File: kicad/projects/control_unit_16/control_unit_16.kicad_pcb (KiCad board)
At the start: 2 copper layers, 203.2 x 97.8 mm, 54 parts, among them J1 Conn_01x04_Female, J2 Control_signal_backplane, J3 Bus_connection, J4 Aux_connection, J5 Conn_01x16_Female, U1 74HCT04, U10 28C256, U11 28C256, U2 28C256, U3 74HCT173, U4 74HCT377, U5 74HCT161, U6 28C256, U7 74HCT245, U8 74HCT245, U9 74HCT138

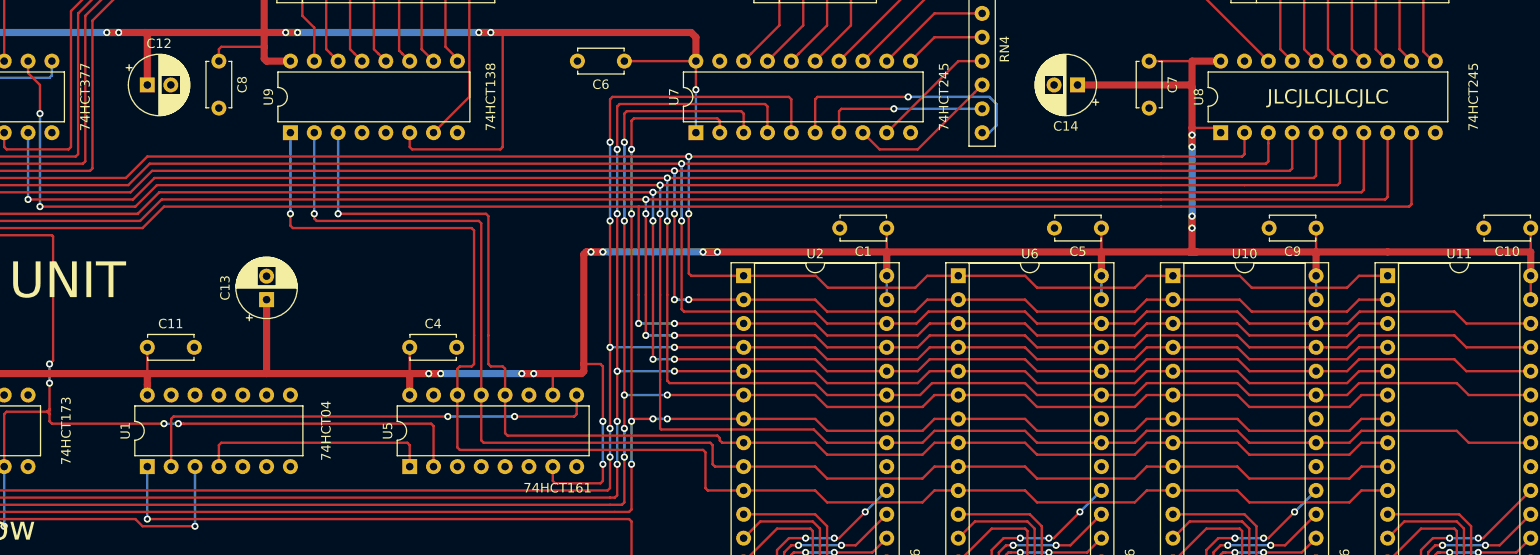
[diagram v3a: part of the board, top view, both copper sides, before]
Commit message: Switch to HC series chips and fix some labelling in program counter or register PCB.
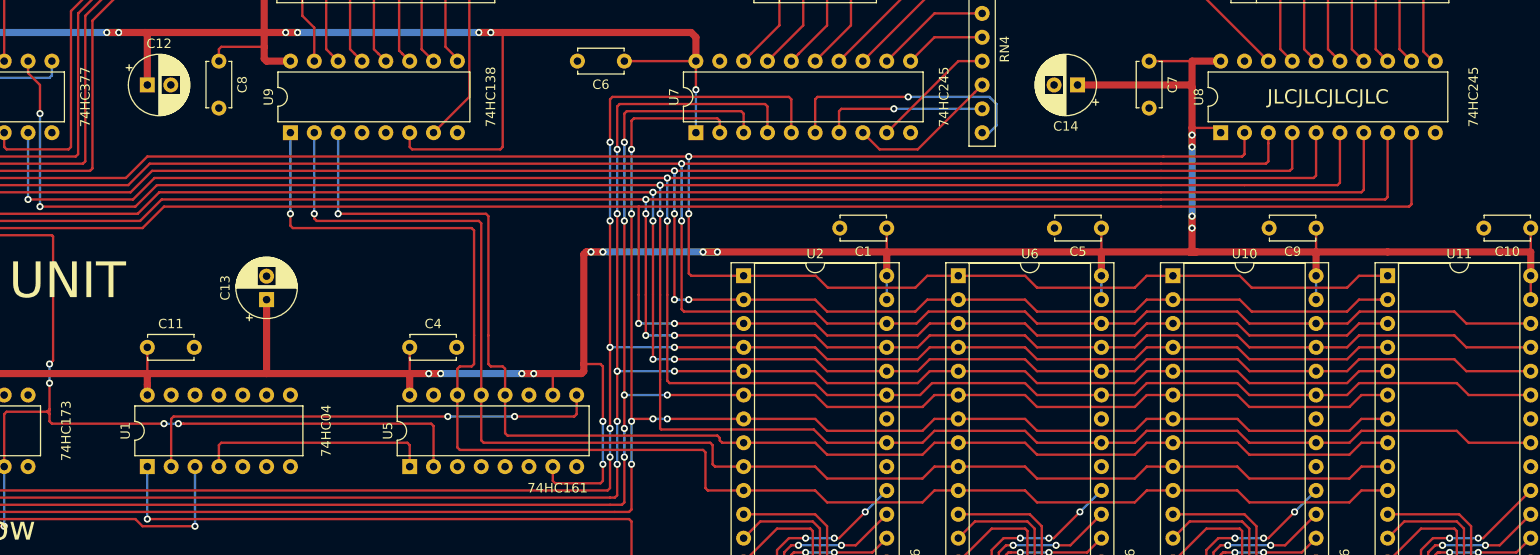
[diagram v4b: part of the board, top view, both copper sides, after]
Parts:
- U1: value 74HCT04 -> 74HC04
- U3: value 74HCT173 -> 74HC173
- U4: value 74HCT377 -> 74HC377
- U5: value 74HCT161 -> 74HC161
- U7, U8: value 74HCT245 -> 74HC245
- U9: value 74HCT138 -> 74HC138
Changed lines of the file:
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@@
       (effects (font (size 1 1) (thickness 0.15)))
     )
-    (fp_text value 74HCT138 (at 3.81 21.336 90) (layer F.SilkS)
+    (fp_text value 74HC138 (at 3.81 21.336 90) (layer F.SilkS)
       (effects (font (size 1.016 1.016) (thickness 0.1778)))
     )
@@
       (effects (font (size 1 1) (thickness 0.15)))
     )
-    (fp_text value 74HCT245 (at 3.81 26.924 90) (layer F.SilkS)
+    (fp_text value 74HC245 (at 3.81 26.924 90) (layer F.SilkS)
       (effects (font (size 1.016 1.016) (thickness 0.1778)))
     )
@@
       (effects (font (size 1 1) (thickness 0.15)))
     )
-    (fp_text value 74HCT245 (at 3.81 26.416 90) (layer F.SilkS)
+    (fp_text value 74HC245 (at 3.81 26.416 90) (layer F.SilkS)
       (effects (font (size 1.016 1.016) (thickness 0.1778)))
     )
@@
       (effects (font (size 1 1) (thickness 0.15)))
     )
-    (fp_text value 74HCT161 (at -2.286 15.748 180) (layer F.SilkS)
+    (fp_text value 74HC161 (at -2.286 15.748 180) (layer F.SilkS)
       (effects (font (size 1.016 1.016) (thickness 0.1778)))
     )
@@
       (effects (font (size 1 1) (thickness 0.15)))
     )
-    (fp_text value 74HCT377 (at 3.81 26.416 90) (layer F.SilkS)
+    (fp_text value 74HC377 (at 3.81 26.416 90) (layer F.SilkS)
       (effects (font (size 1.016 1.016) (thickness 0.1778)))
     )
@@
       (effects (font (size 1 1) (thickness 0.15)))
     )
-    (fp_text value 74HCT173 (at 3.81 21.844 90) (layer F.SilkS)
+    (fp_text value 74HC173 (at 3.81 21.844 90) (layer F.SilkS)
       (effects (font (size 1.016 1.016) (thickness 0.1778)))
     )
@@
       (effects (font (size 1 1) (thickness 0.15)))
     )
-    (fp_text value 74HCT04 (at 3.81 19.05 90) (layer F.SilkS)
-      (effects (font (size 1.016 1.016) (thickness 0.1778)))
-    )
+    (fp_text value 74HC04 (at 3.81 19.05 90) (layer F.SilkS)
+      (effects (font (size 1.016 1.016) (thickness 0.1778)))
+    )

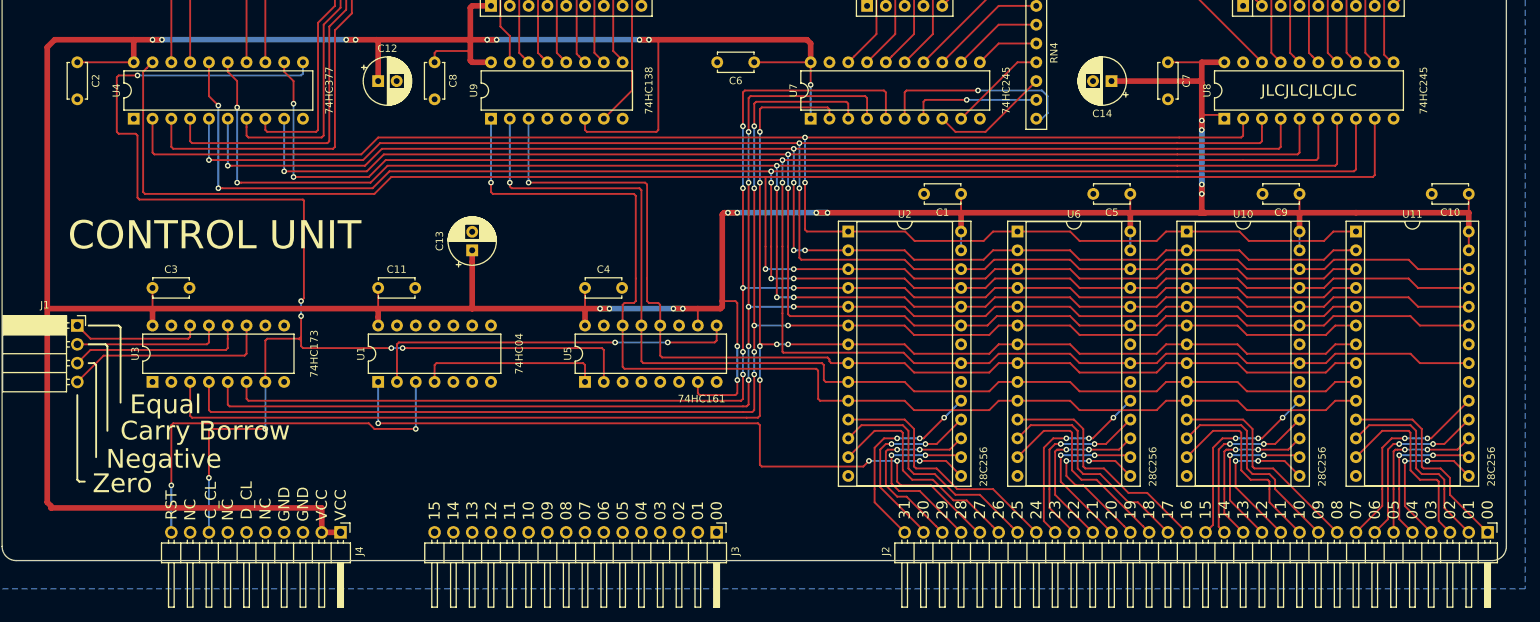
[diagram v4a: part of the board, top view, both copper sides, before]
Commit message: Adjust lower connector position on control unit.
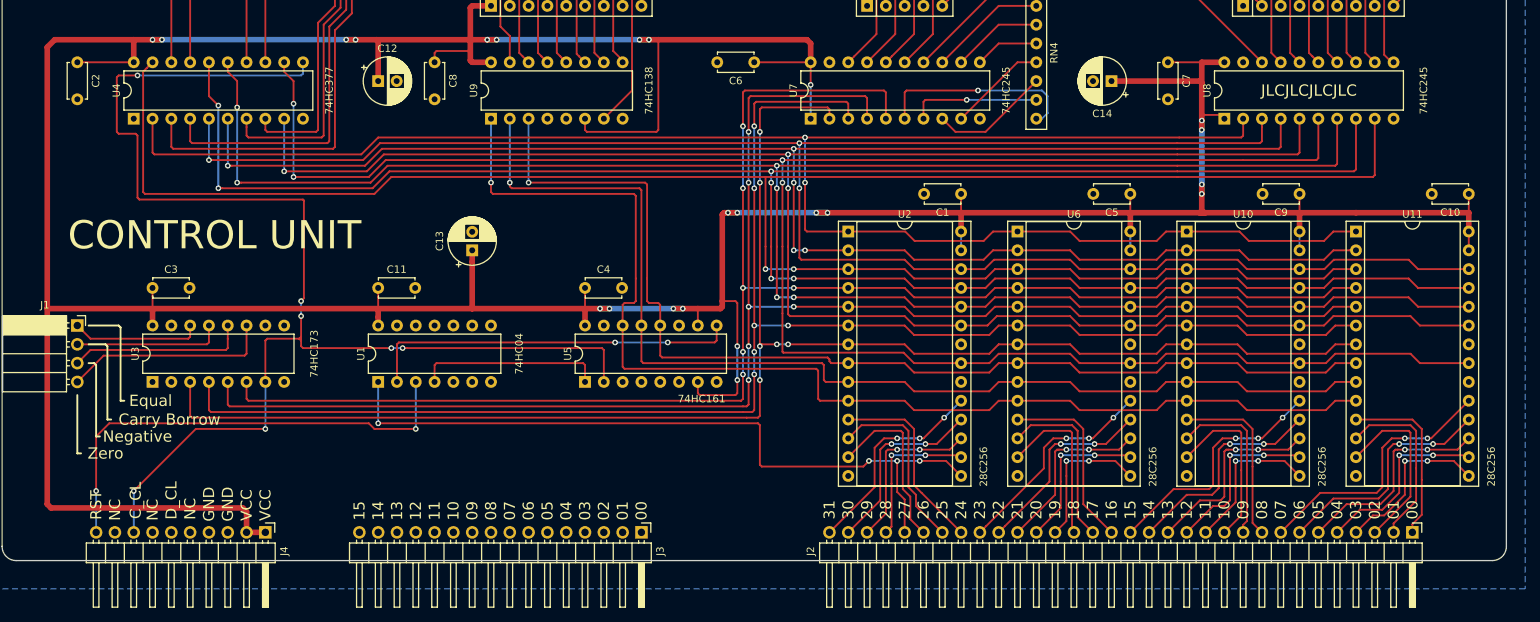
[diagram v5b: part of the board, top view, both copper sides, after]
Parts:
- moved J2 10.2 mm to (241.3, 144.8)
- moved J3 10.2 mm to (137.2, 144.8)
- moved J4 10.2 mm to (86.4, 144.8)
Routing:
- net VCC: track 626.3 -> 615.8 mm
- net /RESET: track 54.3 -> 63.5 mm
- net /ROM_3_0: track 34.7 -> 26.0 mm
- net /ROM_0_7: track 27.2 -> 35.9 mm
- net /ROM_0_6: track 24.5 -> 32.3 mm
- net /ROM_3_1: track 32.6 -> 24.8 mm
- net /ROM_2_0: track 32.1 -> 25.0 mm
- net /ROM_1_7: track 26.2 -> 33.2 mm
- net /ROM_3_2: track 30.5 -> 23.6 mm
- net /ROM_0_5: track 21.8 -> 28.7 mm
- net /STEP_RESET: track 107.8 -> 101.1 mm
- net /ROM_2_1: track 30.0 -> 23.7 mm
- net /ROM_1_0: track 29.6 -> 23.9 mm
- net /ROM_1_6: track 24.1 -> 29.7 mm
- net /CONTROL_CLOCK: track 172.3 -> 177.7 mm
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
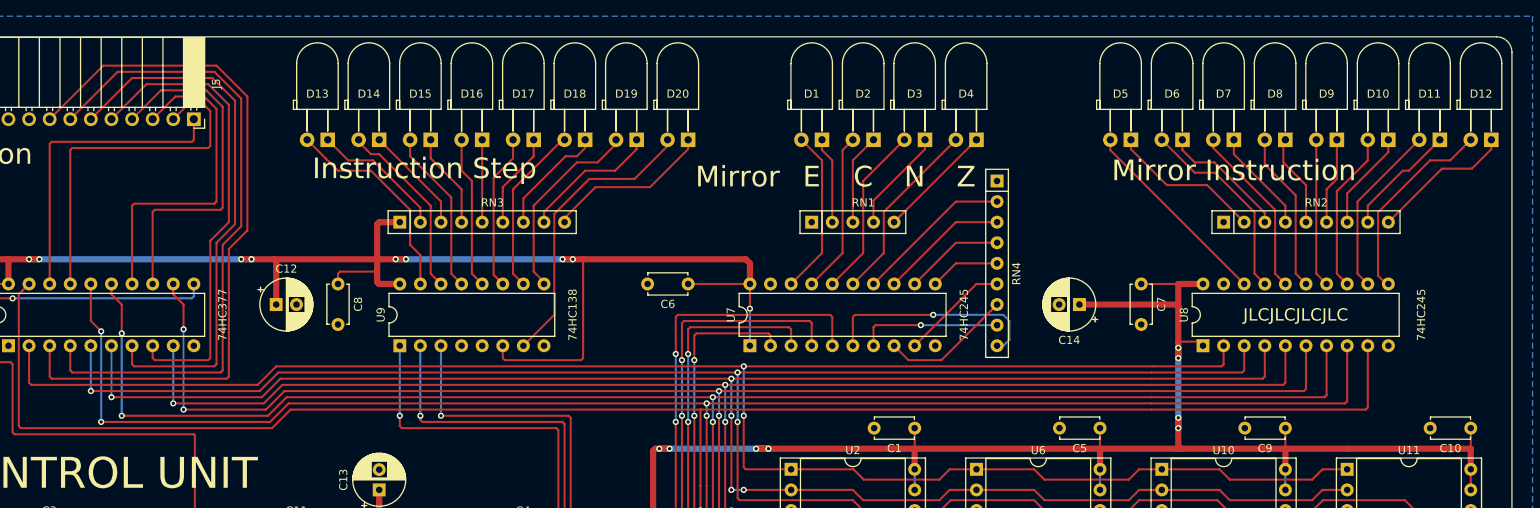
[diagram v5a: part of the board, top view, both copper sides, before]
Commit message: Add top power and LED control to control unit.
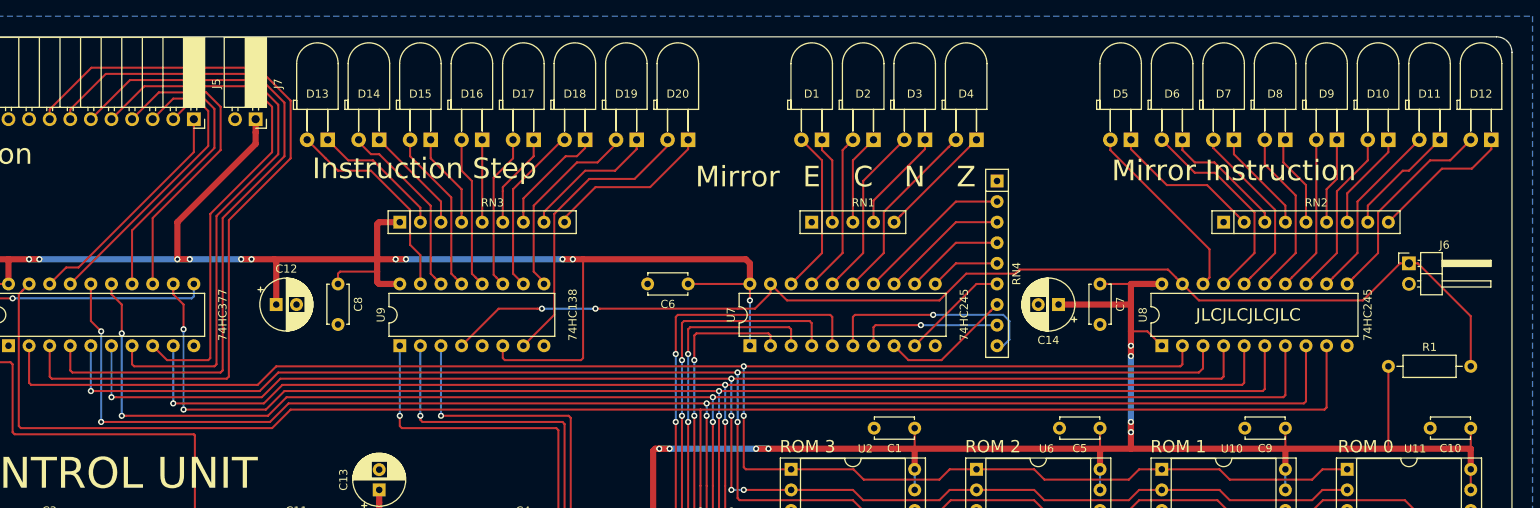
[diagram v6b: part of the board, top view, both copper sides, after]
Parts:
- added J6: LED_CONTROL, Connector_PinHeader_2.54mm:PinHeader_1x02_P2.54mm_Horizontal, F.Cu at (241.3, 78.7)
- added J7: TOP_POWER, Connector_PinSocket_2.54mm:PinSocket_1x02_P2.54mm_Horizontal, F.Cu at (99.1, 61.0)
- added R1: R_US, Resistor_THT:R_Axial_DIN0207_L6.3mm_D2.5mm_P10.16mm_Horizontal, F.Cu at (238.8, 91.4)
- moved C7 5.08 mm to (203.2, 81.3)
- moved U8 5.08 mm to (210.8, 88.9)
- moved C14 2.58 mm to (198.1, 83.8)
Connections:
- U7 pad 19: GND -> /LED_CONTROL
- U8 pad 19: GND -> /LED_CONTROL
- U9 pad 4: GND -> /LED_CONTROL
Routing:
- net /LED_CONTROL: track 0.00 -> 143.1 mm, vias 0 -> 2
- net VCC: track 615.8 -> 645.8 mm, vias 23 -> 25
- net /INST_01: track 44.1 -> 33.8 mm
- net /INST_00: track 37.8 -> 28.6 mm
- net /INST_06: track 81.4 -> 89.1 mm
- net /INST_07: track 90.3 -> 98.0 mm
- net /INST_05: track 67.4 -> 74.4 mm
- net /INST_02: track 41.4 -> 35.0 mm
- net /INST_04: track 58.4 -> 64.6 mm
- net /INST_03: track 43.7 -> 38.3 mm
- net /MIR_INST_6: track 261.6 -> 256.4 mm
- net /MIR_INST_5: track 246.3 -> 241.2 mm
- net /MIR_INST_4: track 267.2 -> 262.1 mm
- net /MIR_INST_2: track 287.5 -> 282.4 mm
- net /MIR_INST_1: track 291.8 -> 286.7 mm
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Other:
- board text added: "ROM 0"
- board text added: "ROM 1"
- board text added: "ROM 2"
- board text added: "ROM 3"

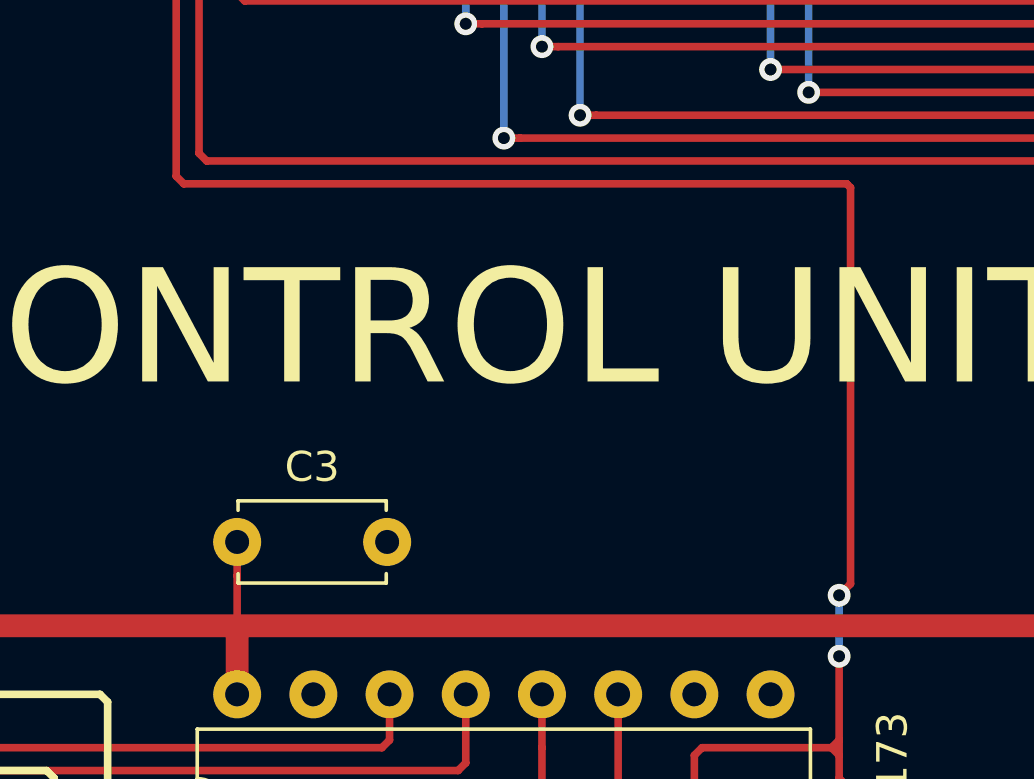
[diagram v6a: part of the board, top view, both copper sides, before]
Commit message: Add top power and LED control to program counter.
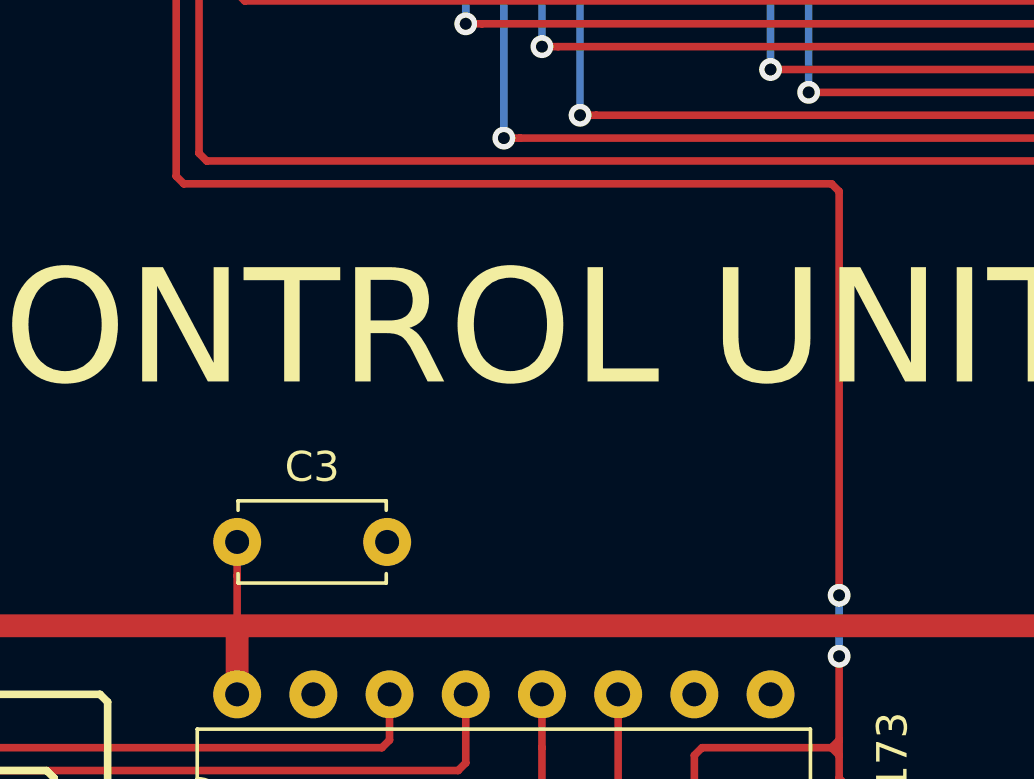
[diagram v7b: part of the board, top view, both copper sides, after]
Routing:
- net /CONTROL_CLOCK: track 177.7 -> 177.1 mm
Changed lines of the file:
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@@
     (thickness 1.6)
     (drawings 40)
-    (tracks 1318)
+    (tracks 1317)
     (zones 0)
     (modules 57)
@@
   (via (at 91.186 113.538) (size 0.762) (drill 0.4) (layers F.Cu B.Cu) (net 98))
   (segment (start 91.186 115.57) (end 91.186 113.538) (width 0.254) (layer B.Cu) (net 98))
-  (segment (start 91.566999 113.157001) (end 91.566999 99.948999) (width 0.254) (layer F.Cu) (net 98))
-  (segment (start 91.186 113.538) (end 91.566999 113.157001) (width 0.254) (layer F.Cu) (net 98))
-  (segment (start 91.566999 99.948999) (end 91.44 99.822) (width 0.254) (layer F.Cu) (net 98))
-  (segment (start 91.44 99.822) (end 69.342 99.822) (width 0.254) (layer F.Cu) (net 98))
-  (segment (start 69.342 99.822) (end 69.088 99.568) (width 0.254) (layer F.Cu) (net 98))
-  (segment (start 69.088 99.568) (end 69.088 91.186) (width 0.254) (layer F.Cu) (net 98))
-  (segment (start 69.088 91.186) (end 68.834 90.932) (width 0.254) (layer F.Cu) (net 98))
-  (segment (start 68.834 90.932) (end 66.548 90.932) (width 0.254) (layer F.Cu) (net 98))
-  (segment (start 66.548 90.932) (end 66.294 90.678) (width 0.254) (layer F.Cu) (net 98))
-  (segment (start 66.294 90.678) (end 66.294 83.312) (width 0.254) (layer F.Cu) (net 98))
-  (segment (start 66.294 83.312) (end 66.548 83.058) (width 0.254) (layer F.Cu) (net 98))
   (via (at 69.088 83.058) (size 0.762) (drill 0.4) (layers F.Cu B.Cu) (net 98))
-  (segment (start 66.548 83.058) (end 69.088 83.058) (width 0.254) (layer F.Cu) (net 98))
   (segment (start 69.088 83.058) (end 91.186 83.058) (width 0.254) (layer B.Cu) (net 98))
   (segment (start 91.186 83.058) (end 91.44 82.804) (width 0.254) (layer B.Cu) (net 98))
@@
   (segment (start 76.962 130.81) (end 68.579992 139.192008) (width 0.254) (layer F.Cu) (net 98))
   (segment (start 68.58 139.192008) (end 68.58 144.78) (width 0.254) (layer B.Cu) (net 98))
+  (segment (start 66.548 90.932) (end 66.294 90.678) (width 0.254) (layer F.Cu) (net 98))
+  (segment (start 91.186 100.076) (end 90.932 99.822) (width 0.254) (layer F.Cu) (net 98))
+  (segment (start 66.294 83.312) (end 66.548 83.058) (width 0.254) (layer F.Cu) (net 98))
+  (segment (start 69.342 99.822) (end 69.088 99.568) (width 0.254) (layer F.Cu) (net 98))
+  (segment (start 69.088 99.568) (end 69.088 91.186) (width 0.254) (layer F.Cu) (net 98))
+  (segment (start 66.548 83.058) (end 69.088 83.058) (width 0.254) (layer F.Cu) (net 98))
+  (segment (start 66.294 90.678) (end 66.294 83.312) (width 0.254) (layer F.Cu) (net 98))
+  (segment (start 68.834 90.932) (end 66.548 90.932) (width 0.254) (layer F.Cu) (net 98))
+  (segment (start 91.186 113.538) (end 91.186 100.076) (width 0.254) (layer F.Cu) (net 98))
+  (segment (start 69.088 91.186) (end 68.834 90.932) (width 0.254) (layer F.Cu) (net 98))
+  (segment (start 90.932 99.822) (end 69.342 99.822) (width 0.254) (layer F.Cu) (net 98))
   (segment (start 106.68 124.46) (end 106.68 130.81) (width 0.254) (layer B.Cu) (net 100))
   (via (at 106.68 130.81) (size 0.762) (drill 0.4) (layers F.Cu B.Cu) (net 100))
